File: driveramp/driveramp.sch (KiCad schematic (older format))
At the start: 49 parts, among them J1 SMA, J2 SMA, P1 FAULT, P2 CONN_2, T1 MABA-011002, T2 2x Fair-Rite 2843006802, coax, U1 LM2936HVBMA-5.0, U2 MRFE6VP100H, U3 TL783

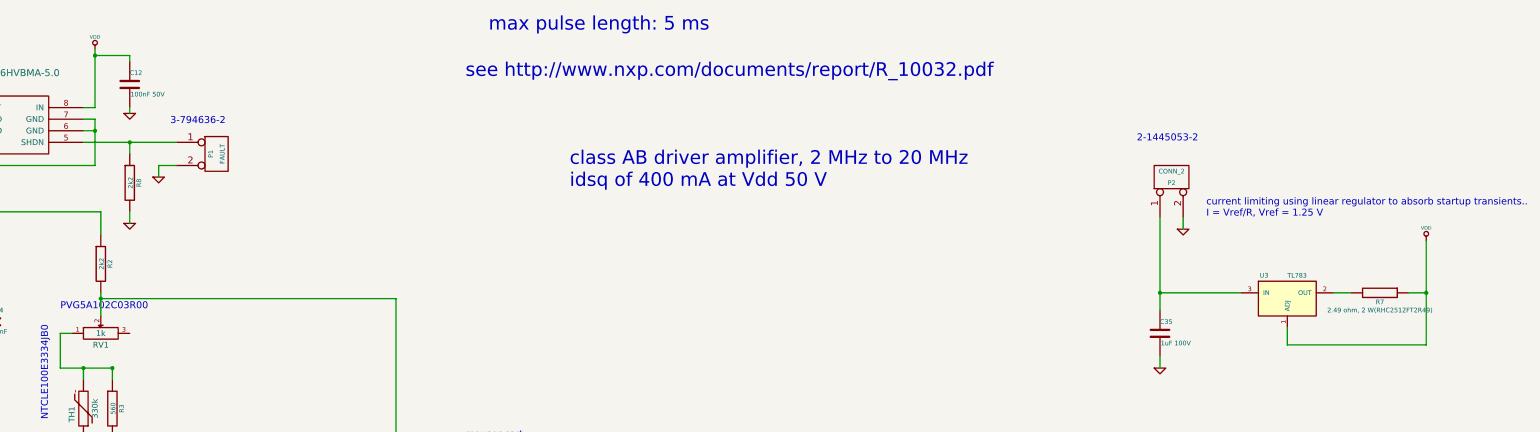
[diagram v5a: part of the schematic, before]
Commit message: switched driver amp current limiter to to-220 lm317hv, heatsink against al plate
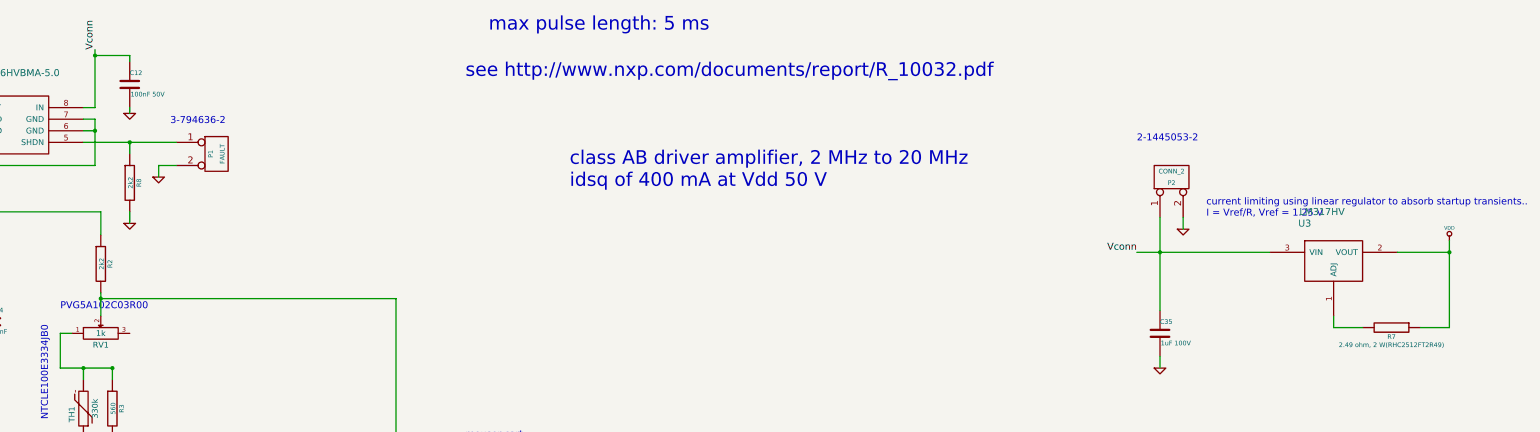
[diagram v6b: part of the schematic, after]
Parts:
- removed U3: TL783, SMD_Packages:DPAK3, symbol LM317AMDT
- added U3: LM317HV, symbol LM317HV
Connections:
- net VDD: now also U3.2 (VOUT); no longer C12.1, U1.8 (IN)
- net Vconn: now reaches C35.1, P2.1 (P1)
- net Vconn: now also C12.1, U1.8 (IN), U3.3 (VIN)
- net at R7.2: now also U3.1 (ADJ)
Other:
- moved on the sheet: R7

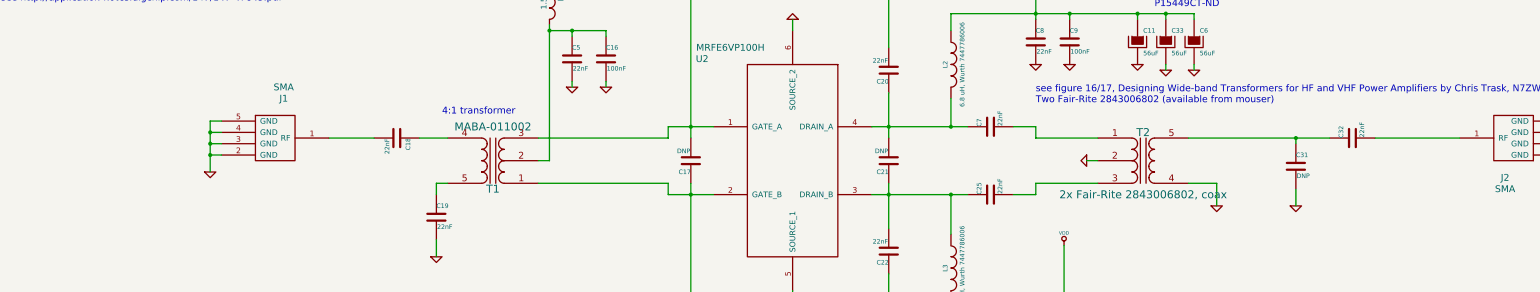
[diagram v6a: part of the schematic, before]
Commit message: added matching network on driver amp board, modified footprint on transformer for easier soldering
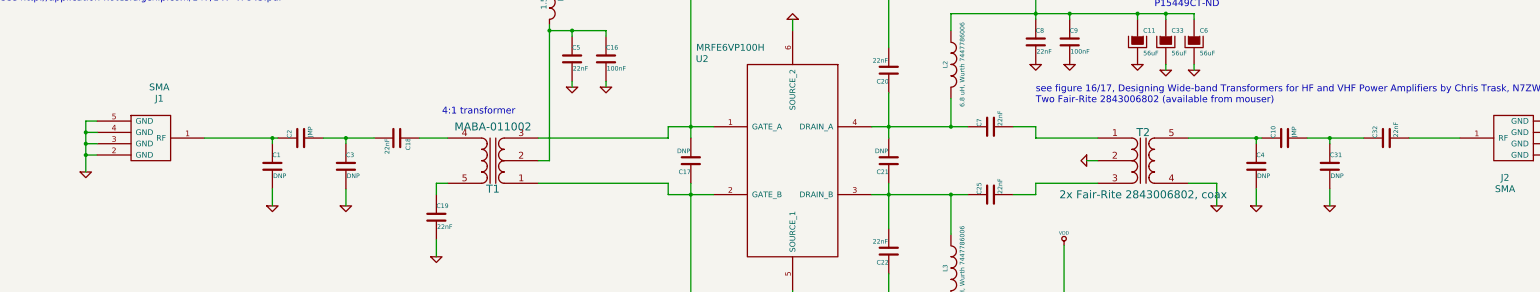
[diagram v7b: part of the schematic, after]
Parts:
- added C1, C3, C4: DNP, Capacitors_SMD:c_0805, symbol C
- added C10, C2: JMP, Capacitors_SMD:c_0805, symbol C
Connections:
- net GND: now also C1.2, C3.2, C4.2
- net at J1.1 (RF): now also C1.1, C2.1; no longer C18.2
- net at C31.1, C32.1: now also C10.2; no longer T2.5 (S2)
- new net: C18.2, C2.2, C3.1
- new net: C10.1, C4.1, T2.5 (S2)
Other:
- moved on the sheet: C31, C32, J1

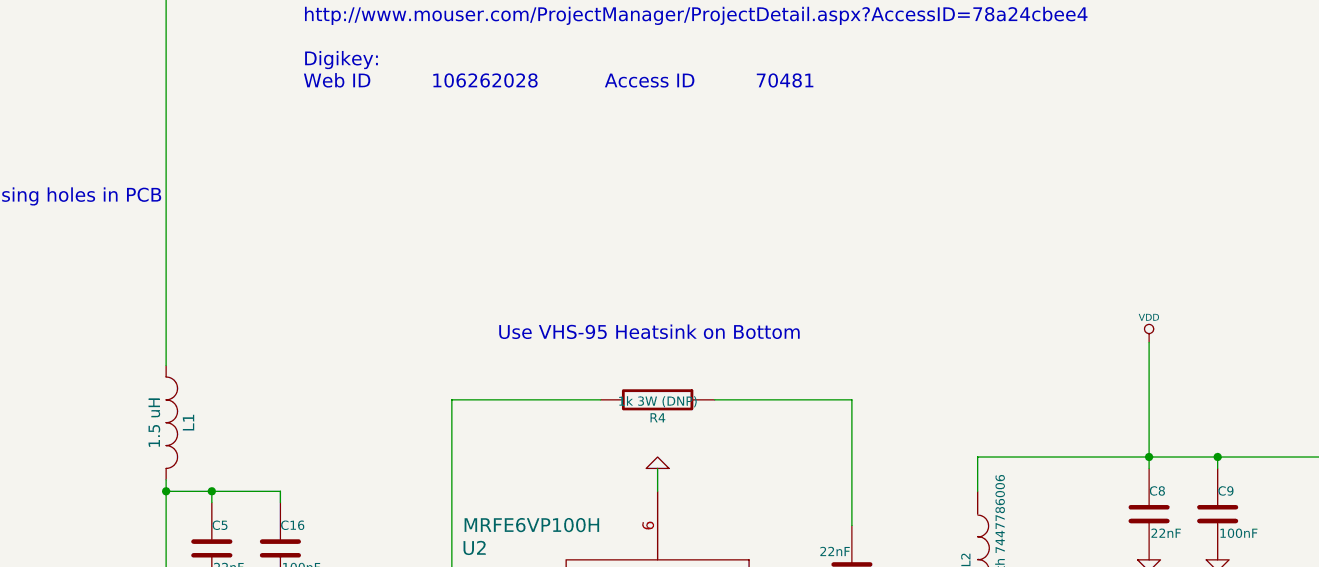
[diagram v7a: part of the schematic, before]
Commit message: added extra decoupling to driver amp bias, specified fet ground connection
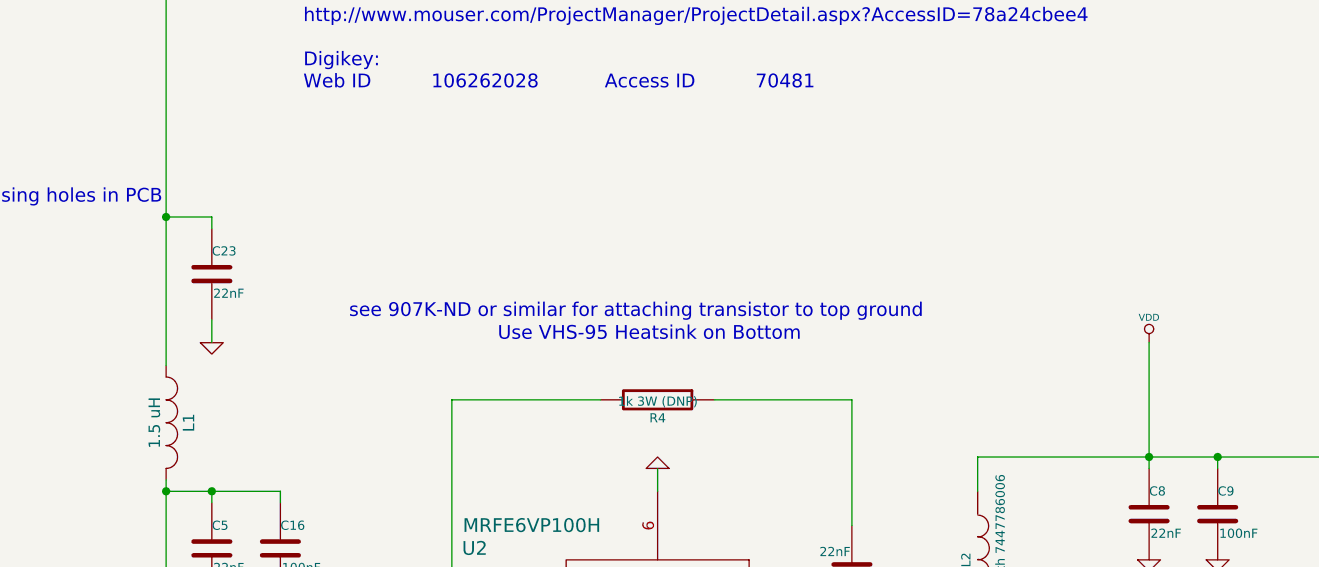
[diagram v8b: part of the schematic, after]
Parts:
- added C23: 22nF, Capacitors_SMD:c_0805, symbol C
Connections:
- net GND: now also C23.2
- net at L1.1, R2.2, RV1.2: now also C23.1
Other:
- note added: "see 907K-ND or similar for attaching transistor to top ground"
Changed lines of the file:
@@
 $EndComp
 $Comp
-L GND #PWR21
+L GND #PWR22
 U 1 1 529EC2FF
 P 10550 7100
-F 0 "#PWR21" H 10550 7100 30  0001 C CNN
+F 0 "#PWR22" H 10550 7100 30  0001 C CNN
 F 1 "GND" H 10550 7030 30  0001 C CNN
 F 2 "" H 10550 7100 60  0000 C CNN
@@
 $EndComp
 $Comp
-L GND #PWR18
+L GND #PWR19
 U 1 1 529EC31D
 P 9950 7100
-F 0 "#PWR18" H 9950 7100 30  0001 C CNN
+F 0 "#PWR19" H 9950 7100 30  0001 C CNN
 F 1 "GND" H 9950 7030 30  0001 C CNN
 F 2 "" H 9950 7100 60  0000 C CNN
@@
 $EndComp
 $Comp
-L GND #PWR15
+L GND #PWR16
 U 1 1 529EC32C
 P 9650 7100
-F 0 "#PWR15" H 9650 7100 30  0001 C CNN
+F 0 "#PWR16" H 9650 7100 30  0001 C CNN
 F 1 "GND" H 9650 7030 30  0001 C CNN
 F 2 "" H 9650 7100 60  0000 C CNN
@@
 $EndComp
 $Comp
-L GND #PWR34
+L GND #PWR35
 U 1 1 529EC8CC
 P 14450 8100
-F 0 "#PWR34" H 14450 8100 30  0001 C CNN
+F 0 "#PWR35" H 14450 8100 30  0001 C CNN
 F 1 "GND" H 14450 8030 30  0001 C CNN
 F 2 "" H 14450 8100 60  0000 C CNN
@@
 $EndComp
 $Comp
-L GND #PWR31
+L GND #PWR32
 U 1 1 5346E112
 P 12150 2850
-F 0 "#PWR31" H 12150 2850 30  0001 C CNN
+F 0 "#PWR32" H 12150 2850 30  0001 C CNN
 F 1 "GND" H 12150 2780 30  0001 C CNN
 F 2 "" H 12150 2850 60  0000 C CNN
@@
 $EndComp
 $Comp
-L VDD #PWR14
+L VDD #PWR15
 U 1 1 53862298
 P 9650 6150
-F 0 "#PWR14" H 9650 6250 30  0001 C CNN
+F 0 "#PWR15" H 9650 6250 30  0001 C CNN
 F 1 "VDD" H 9650 6260 30  0000 C CNN
 F 2 "" H 9650 6150 60  0000 C CNN
@@
 $EndComp
 $Comp
-L GND #PWR19
+L GND #PWR20
 U 1 1 53A9A63B
 P 10100 7950
-F 0 "#PWR19" H 10100 7950 30  0001 C CNN
+F 0 "#PWR20" H 10100 7950 30  0001 C CNN
 F 1 "GND" H 10100 7880 30  0001 C CNN
 F 2 "" H 10100 7950 60  0000 C CNN
@@
 $EndComp
 $Comp
-L GND #PWR13
+L GND #PWR14
 U 1 1 53A9D043
 P 7500 9200
-F 0 "#PWR13" H 7500 9200 30  0001 C CNN
+F 0 "#PWR14" H 7500 9200 30  0001 C CNN
 F 1 "GND" H 7500 9130 30  0001 C CNN
 F 2 "" H 7500 9200 60  0000 C CNN
@@
 $EndComp
 $Comp
-L GND #PWR12
+L GND #PWR13
 U 1 1 53A9D226
 P 7500 6700
-F 0 "#PWR12" H 7500 6700 30  0001 C CNN
+F 0 "#PWR13" H 7500 6700 30  0001 C CNN
 F 1 "GND" H 7500 6630 30  0001 C CNN
 F 2 "" H 7500 6700 60  0000 C CNN
@@
 $EndComp
 $Comp
-L GND #PWR10
+L GND #PWR11
 U 1 1 53A9F0C3
 P 5550 7300
-F 0 "#PWR10" H 5550 7300 30  0001 C CNN
+F 0 "#PWR11" H 5550 7300 30  0001 C CNN
 F 1 "GND" H 5550 7230 30  0001 C CNN
 F 2 "" H 5550 7300 60  0000 C CNN
@@
 $EndComp
 $Comp
-L GND #PWR11
+L GND #PWR12
 U 1 1 53A9F3B0
 P 5850 7300
-F 0 "#PWR11" H 5850 7300 30  0001 C CNN
+F 0 "#PWR12" H 5850 7300 30  0001 C CNN
 F 1 "GND" H 5850 7230 30  0001 C CNN
 F 2 "" H 5850 7300 60  0000 C CNN
@@
 $EndComp
 $Comp
-L GND #PWR23
+L GND #PWR24
 U 1 1 53A9FA93
 P 10800 9900
-F 0 "#PWR23" H 10800 9900 30  0001 C CNN
+F 0 "#PWR24" H 10800 9900 30  0001 C CNN
 F 1 "GND" H 10800 9830 30  0001 C CNN
 F 2 "" H 10800 9900 60  0000 C CNN
@@
 $EndComp
 $Comp
-L GND #PWR20
+L GND #PWR21
 U 1 1 53A9FA9F
 P 10200 9900
-F 0 "#PWR20" H 10200 9900 30  0001 C CNN
+F 0 "#PWR21" H 10200 9900 30  0001 C CNN
 F 1 "GND" H 10200 9830 30  0001 C CNN
 F 2 "" H 10200 9900 60  0000 C CNN
@@
 $EndComp
 $Comp
-L GND #PWR17
+L GND #PWR18
 U 1 1 53A9FAA5
 P 9900 9900
-F 0 "#PWR17" H 9900 9900 30  0001 C CNN
+F 0 "#PWR18" H 9900 9900 30  0001 C CNN
 F 1 "GND" H 9900 9830 30  0001 C CNN
 F 2 "" H 9900 9900 60  0000 C CNN
@@
 $EndComp
 $Comp
-L GND #PWR26
+L GND #PWR27
 U 1 1 53AA02AE
 P 11250 8350
-F 0 "#PWR26" H 11250 8350 30  0001 C CNN
+F 0 "#PWR27" H 11250 8350 30  0001 C CNN
 F 1 "GND" H 11250 8280 30  0001 C CNN
 F 2 "" H 11250 8350 60  0000 C CNN
@@
 $EndComp
 $Comp
-L GND #PWR32
+L GND #PWR33
 U 1 1 53AA09E5
 P 12250 8350
-F 0 "#PWR32" H 12250 8350 30  0001 C CNN
+F 0 "#PWR33" H 12250 8350 30  0001 C CNN
 F 1 "GND" H 12250 8280 30  0001 C CNN
 F 2 "" H 12250 8350 60  0000 C CNN
@@
 $EndComp
 $Comp
-L VDD #PWR33
+L VDD #PWR34
 U 1 1 53A9D510
 P 14450 2950
-F 0 "#PWR33" H 14450 3050 30  0001 C CNN
+F 0 "#PWR34" H 14450 3050 30  0001 C CNN
 F 1 "VDD" H 14450 3060 30  0000 C CNN
 F 2 "" H 14450 2950 60  0000 C CNN
@@
 $EndComp
 $Comp
-L GND #PWR29
+L GND #PWR30
 U 1 1 53A9D5F1
 P 11650 10300
-F 0 "#PWR29" H 11650 10300 30  0001 C CNN
+F 0 "#PWR30" H 11650 10300 30  0001 C CNN
 F 1 "GND" H 11650 10230 30  0001 C CNN
 F 2 "" H 11650 10300 60  0000 C CNN
@@
 $EndComp
 $Comp
-L GND #PWR25
+L GND #PWR26
 U 1 1 53A9F715
 P 11100 9950
-F 0 "#PWR25" H 11100 9950 30  0001 C CNN
+F 0 "#PWR26" H 11100 9950 30  0001 C CNN
 F 1 "GND" H 11100 9880 30  0001 C CNN
 F 2 "" H 11100 9950 60  0000 C CNN
@@
 $EndComp
 $Comp
-L GND #PWR22
+L GND #PWR23
 U 1 1 53A9FBE6
 P 10800 7150
-F 0 "#PWR22" H 10800 7150 30  0001 C CNN
+F 0 "#PWR23" H 10800 7150 30  0001 C CNN
 F 1 "GND" H 10800 7080 30  0001 C CNN
 F 2 "" H 10800 7150 60  0000 C CNN
@@
 $EndComp
 $Comp
-L VDD #PWR16
+L VDD #PWR17
 U 1 1 53AA1331
 P 9900 8700
-F 0 "#PWR16" H 9900 8800 30  0001 C CNN
+F 0 "#PWR17" H 9900 8800 30  0001 C CNN
 F 1 "VDD" H 9900 8810 30  0000 C CNN
 F 2 "" H 9900 8700 60  0000 C CNN
@@
 3-794636-2
 $Comp
-L GND #PWR30
+L GND #PWR31
 U 1 1 53CF64AD
 P 11950 4050
-F 0 "#PWR30" H 11950 4050 30  0001 C CNN
+F 0 "#PWR31" H 11950 4050 30  0001 C CNN
 F 1 "GND" H 11950 3980 30  0001 C CNN
 F 2 "" H 11950 4050 60  0000 C CNN
@@
 $EndComp
 $Comp
-L GND #PWR24
+L GND #PWR25
 U 1 1 53CFF43B
 P 11050 7150
-F 0 "#PWR24" H 11050 7150 30  0001 C CNN
+F 0 "#PWR25" H 11050 7150 30  0001 C CNN
 F 1 "GND" H 11050 7080 30  0001 C CNN
 F 2 "" H 11050 7150 60  0000 C CNN
@@
 $EndComp
 $Comp
-L GND #PWR27
+L GND #PWR28
 U 1 1 53CFF451
 P 11350 9950
-F 0 "#PWR27" H 11350 9950 30  0001 C CNN
+F 0 "#PWR28" H 11350 9950 30  0001 C CNN
 F 1 "GND" H 11350 9880 30  0001 C CNN
 F 2 "" H 11350 9950 60  0000 C CNN
@@
 $EndComp
 $Comp
-L GND #PWR28
+L GND #PWR29
 U 1 1 5494AD14
 P 11600 8350
-F 0 "#PWR28" H 11600 8350 30  0001 C CNN
+F 0 "#PWR29" H 11600 8350 30  0001 C CNN
 F 1 "GND" H 11600 8280 30  0001 C CNN
 F 2 "" H 11600 8350 60  0000 C CNN
@@
 Wire Wire Line
 	3350 7750 3800 7750
+$Comp
+L C C23
+U 1 1 5494C0A1
+P 5550 5850
+F 0 "C23" H 5550 5950 40  0000 L CNN
+F 1 "22nF" H 5556 5765 40  0000 L CNN
+F 2 "Capacitors_SMD:c_0805" H 5588 5700 30  0001 C CNN
+F 3 "~" H 5550 5850 60  0000 C CNN
+	1    5550 5850
+	1    0    0    -1
+$EndComp
+$Comp
+L GND #PWR10
+U 1 1 5494C0B2
+P 5550 6150
+F 0 "#PWR10" H 5550 6150 30  0001 C CNN
+F 1 "GND" H 5550 6080 30  0001 C CNN
+F 2 "" H 5550 6150 60  0000 C CNN
+F 3 "" H 5550 6150 60  0000 C CNN
+	1    5550 6150
+	1    0    0    -1
+$EndComp
+Wire Wire Line
+	5550 6050 5550 6150
+Wire Wire Line
+	5550 5650 5550 5600
+Wire Wire Line
+	5550 5600 5350 5600
+Connection ~ 5350 5600
+Text Notes 6150 6050 0    60   ~ 0
+see 907K-ND or similar for attaching transistor to top ground
 $EndSCHEMATC
